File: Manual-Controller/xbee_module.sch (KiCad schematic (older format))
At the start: 7 parts, among them U7 TXB0104D, U8 XBee_SMT

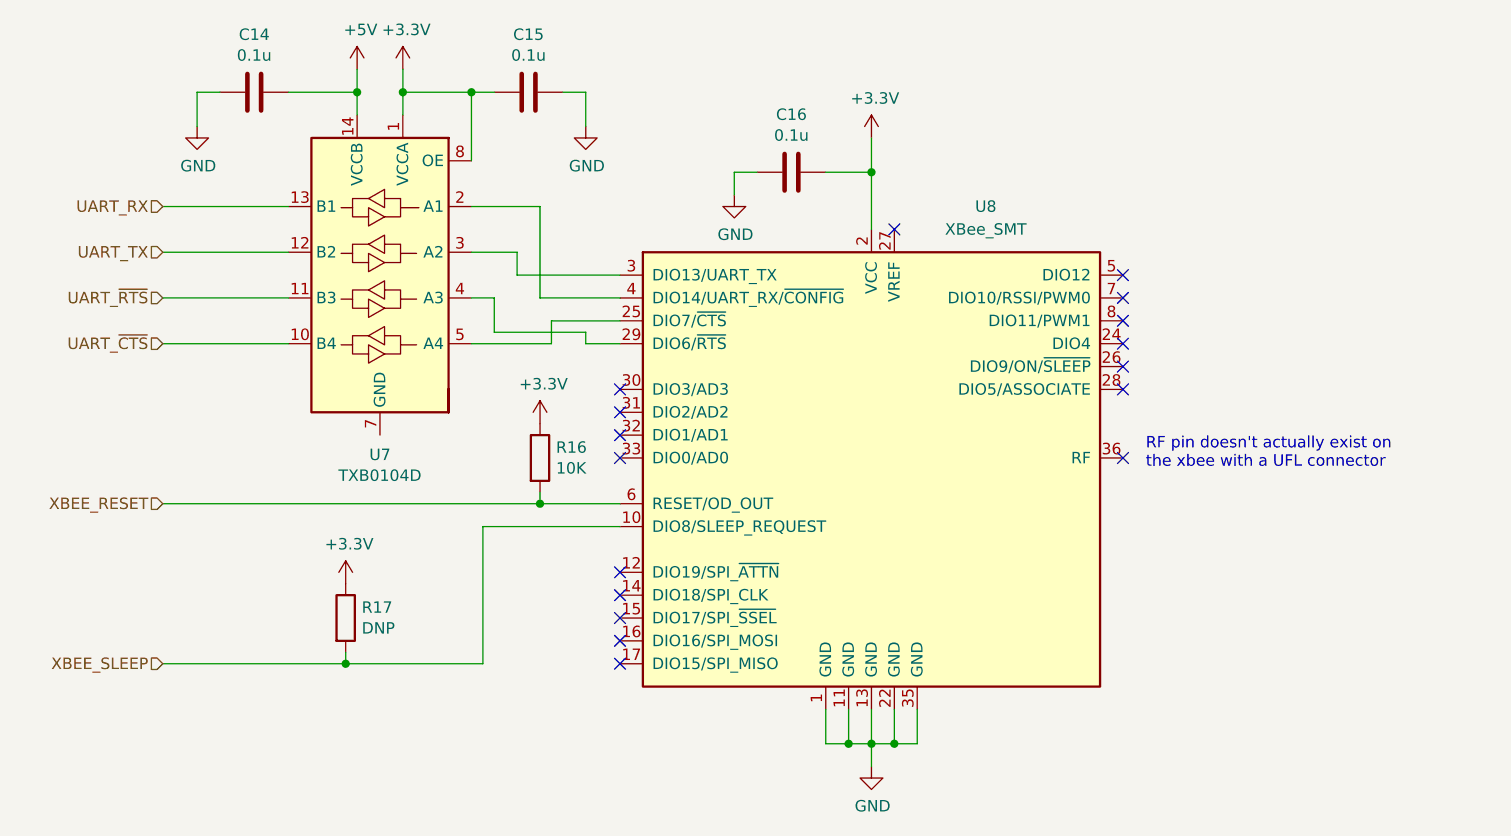
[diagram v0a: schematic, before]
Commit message: assined footprints and fixed pins
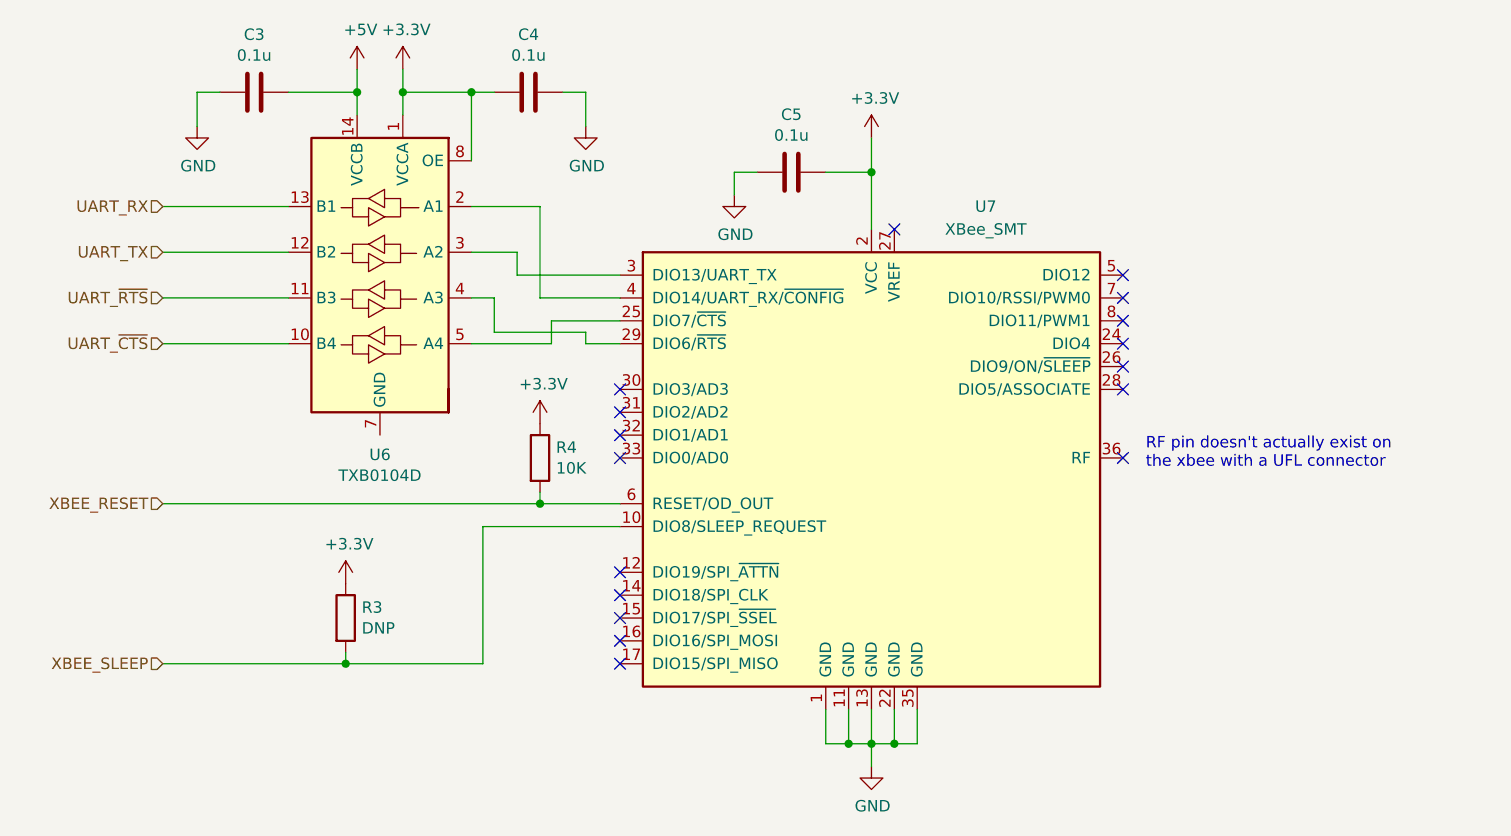
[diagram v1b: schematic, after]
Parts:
- C3: renamed from C14; footprint Capacitor_SMD:C_0805_2012Metric_Pad1.15x1.40mm_HandSolder -> Capacitor_SMD:C_0805_2012Metric_Pad1.18x1.45mm_HandSolder
- C4: renamed from C15; footprint Capacitor_SMD:C_0805_2012Metric_Pad1.15x1.40mm_HandSolder -> Capacitor_SMD:C_0805_2012Metric_Pad1.18x1.45mm_HandSolder
- C5: renamed from C16; footprint Capacitor_SMD:C_0805_2012Metric_Pad1.15x1.40mm_HandSolder -> Capacitor_SMD:C_0805_2012Metric_Pad1.18x1.45mm_HandSolder
- R3: renamed from R17; footprint Resistor_SMD:R_0805_2012Metric_Pad1.15x1.40mm_HandSolder -> Resistor_SMD:R_0805_2012Metric_Pad1.20x1.40mm_HandSolder
- R4: renamed from R16; footprint Resistor_SMD:R_0805_2012Metric_Pad1.15x1.40mm_HandSolder -> Resistor_SMD:R_0805_2012Metric_Pad1.20x1.40mm_HandSolder
- renumbered U7 to U6, U8 to U7
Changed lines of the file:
@@
 $Descr A4 11693 8268
 encoding utf-8
-Sheet 1 2
+Sheet 2 2
 Title ""
 Date ""
@@
 $EndDescr
 $Comp
-L RF_ZigBee:XBee_SMT U8
+L RF_ZigBee:XBee_SMT U7
 U 1 1 5BA27C8A
 P 6150 4250
-F 0 "U8" H 6650 5350 50  0000 C CNN
+F 0 "U7" H 6650 5350 50  0000 C CNN
 F 1 "XBee_SMT" H 6650 5250 50  0000 C CNN
 F 2 "RF_Module:Digi_XBee_SMT" H 6990 3190 50  0001 C CNN
@@
 $EndComp
 $Comp
-L Logic_LevelTranslator:TXB0104D U7
+L Logic_LevelTranslator:TXB0104D U6
 U 1 1 5BA28032
 P 4000 3450
-F 0 "U7" H 4000 2664 50  0000 C CNN
+F 0 "U6" H 4000 2664 50  0000 C CNN
 F 1 "TXB0104D" H 4000 2573 50  0000 C CNN
 F 2 "Package_SO:SOIC-14_3.9x8.7mm_P1.27mm" H 4000 2700 50  0001 C CNN
@@
 $EndComp
 $Comp
-L power:+3.3V #PWR048
+L power:+3.3V #PWR027
 U 1 1 5BA280E0
 P 4100 2550
-F 0 "#PWR048" H 4100 2400 50  0001 C CNN
+F 0 "#PWR027" H 4100 2400 50  0001 C CNN
 F 1 "+3.3V" H 4115 2723 50  0000 C CNN
 F 2 "" H 4100 2550 50  0001 C CNN
@@
 Connection ~ 4100 2650
 $Comp
-L power:+5V #PWR047
+L power:+5V #PWR026
 U 1 1 5BA28183
 P 3900 2550
-F 0 "#PWR047" H 3900 2400 50  0001 C CNN
+F 0 "#PWR026" H 3900 2400 50  0001 C CNN
 F 1 "+5V" H 3915 2723 50  0000 C CNN
 F 2 "" H 3900 2550 50  0001 C CNN
@@
 $EndComp
 $Comp
-L Device:C C15
+L Device:C C4
 U 1 1 5BA281C0
 P 4650 2650
-F 0 "C15" V 4398 2650 50  0000 C CNN
+F 0 "C4" V 4398 2650 50  0000 C CNN
 F 1 "0.1u" V 4489 2650 50  0000 C CNN
-F 2 "Capacitor_SMD:C_0805_2012Metric_Pad1.15x1.40mm_HandSolder" H 4688 2500 50  0001 C CNN
+F 2 "Capacitor_SMD:C_0805_2012Metric_Pad1.18x1.45mm_HandSolder" H 4688 2500 50  0001 C CNN
 F 3 "~" H 4650 2650 50  0001 C CNN
 	1    4650 2650
@@
 $EndComp
 $Comp
-L power:GND #PWR050
+L power:GND #PWR029
 U 1 1 5BA2824E
 P 4900 2800
-F 0 "#PWR050" H 4900 2550 50  0001 C CNN
+F 0 "#PWR029" H 4900 2550 50  0001 C CNN
 F 1 "GND" H 4905 2627 50  0000 C CNN
 F 2 "" H 4900 2800 50  0001 C CNN
@@
 Connection ~ 4400 2650
 $Comp
-L Device:C C14
+L Device:C C3
 U 1 1 5BA282BA
 P 3450 2650
-F 0 "C14" V 3198 2650 50  0000 C CNN
+F 0 "C3" V 3198 2650 50  0000 C CNN
 F 1 "0.1u" V 3289 2650 50  0000 C CNN
-F 2 "Capacitor_SMD:C_0805_2012Metric_Pad1.15x1.40mm_HandSolder" H 3488 2500 50  0001 C CNN
+F 2 "Capacitor_SMD:C_0805_2012Metric_Pad1.18x1.45mm_HandSolder" H 3488 2500 50  0001 C CNN
 F 3 "~" H 3450 2650 50  0001 C CNN
 	1    3450 2650
@@
 $EndComp
 $Comp
-L power:GND #PWR049
+L power:GND #PWR024
 U 1 1 5BA282FE
 P 3200 2800
-F 0 "#PWR049" H 3200 2550 50  0001 C CNN
+F 0 "#PWR024" H 3200 2550 50  0001 C CNN
 F 1 "GND" H 3205 2627 50  0000 C CNN
 F 2 "" H 3200 2800 50  0001 C CNN
@@
 NoConn ~ 6250 3250
 $Comp
-L power:+3.3V #PWR051
+L power:+3.3V #PWR031
 U 1 1 5BA28D48
 P 6150 2850
-F 0 "#PWR051" H 6150 2700 50  0001 C CNN
+F 0 "#PWR031" H 6150 2700 50  0001 C CNN
 F 1 "+3.3V" H 6165 3023 50  0000 C CNN
 F 2 "" H 6150 2850 50  0001 C CNN
@@
 NoConn ~ 7250 3450
 $Comp
-L power:GND #PWR055
+L power:GND #PWR032
 U 1 1 5BA2AF15
 P 6150 5600
-F 0 "#PWR055" H 6150 5350 50  0001 C CNN
+F 0 "#PWR032" H 6150 5350 50  0001 C CNN
 F 1 "GND" H 6155 5427 50  0000 C CNN
 F 2 "" H 6150 5600 50  0001 C CNN
@@
 	3050 3150 3600 3150
 $Comp
-L Device:R R16
+L Device:R R4
 U 1 1 5BA2D660
 P 4700 4250
-F 0 "R16" H 4770 4296 50  0000 L CNN
+F 0 "R4" H 4770 4296 50  0000 L CNN
 F 1 "10K" H 4770 4205 50  0000 L CNN
-F 2 "Resistor_SMD:R_0805_2012Metric_Pad1.15x1.40mm_HandSolder" V 4630 4250 50  0001 C CNN
+F 2 "Resistor_SMD:R_0805_2012Metric_Pad1.20x1.40mm_HandSolder" V 4630 4250 50  0001 C CNN
 F 3 "~" H 4700 4250 50  0001 C CNN
 	1    4700 4250
@@
 $EndComp
 $Comp
-L power:+3.3V #PWR053
+L power:+3.3V #PWR028
 U 1 1 5BA2D6C9
 P 4700 4100
-F 0 "#PWR053" H 4700 3950 50  0001 C CNN
+F 0 "#PWR028" H 4700 3950 50  0001 C CNN
 F 1 "+3.3V" H 4715 4273 50  0000 C CNN
 F 2 "" H 4700 4100 50  0001 C CNN
@@
 NoConn ~ 7250 3850
 $Comp
-L Device:R R17
+L Device:R R3
 U 1 1 5BA2F17A
 P 3850 4950
-F 0 "R17" H 3920 4996 50  0000 L CNN
+F 0 "R3" H 3920 4996 50  0000 L CNN
 F 1 "DNP" H 3920 4905 50  0000 L CNN
-F 2 "Resistor_SMD:R_0805_2012Metric_Pad1.15x1.40mm_HandSolder" V 3780 4950 50  0001 C CNN
+F 2 "Resistor_SMD:R_0805_2012Metric_Pad1.20x1.40mm_HandSolder" V 3780 4950 50  0001 C CNN
 F 3 "~" H 3850 4950 50  0001 C CNN
 	1    3850 4950
@@
 $EndComp
 $Comp
-L power:+3.3V #PWR054
+L power:+3.3V #PWR025
 U 1 1 5BA2F202
 P 3850 4800
-F 0 "#PWR054" H 3850 4650 50  0001 C CNN
+F 0 "#PWR025" H 3850 4650 50  0001 C CNN
 F 1 "+3.3V" H 3865 4973 50  0000 C CNN
 F 2 "" H 3850 4800 50  0001 C CNN
@@
 Connection ~ 3850 5150
 $Comp
-L Device:C C16
+L Device:C C5
 U 1 1 5B9F00A1
 P 5800 3000
-F 0 "C16" V 5548 3000 50  0000 C CNN
+F 0 "C5" V 5548 3000 50  0000 C CNN
 F 1 "0.1u" V 5639 3000 50  0000 C CNN
-F 2 "Capacitor_SMD:C_0805_2012Metric_Pad1.15x1.40mm_HandSolder" H 5838 2850 50  0001 C CNN
+F 2 "Capacitor_SMD:C_0805_2012Metric_Pad1.18x1.45mm_HandSolder" H 5838 2850 50  0001 C CNN
 F 3 "~" H 5800 3000 50  0001 C CNN
 	1    5800 3000
@@
 	6150 3000 6150 3250
 $Comp
-L power:GND #PWR052
+L power:GND #PWR030
 U 1 1 5B9F12A1
 P 5550 3100
-F 0 "#PWR052" H 5550 2850 50  0001 C CNN
+F 0 "#PWR030" H 5550 2850 50  0001 C CNN
 F 1 "GND" H 5555 2927 50  0000 C CNN
 F 2 "" H 5550 3100 50  0001 C CNN

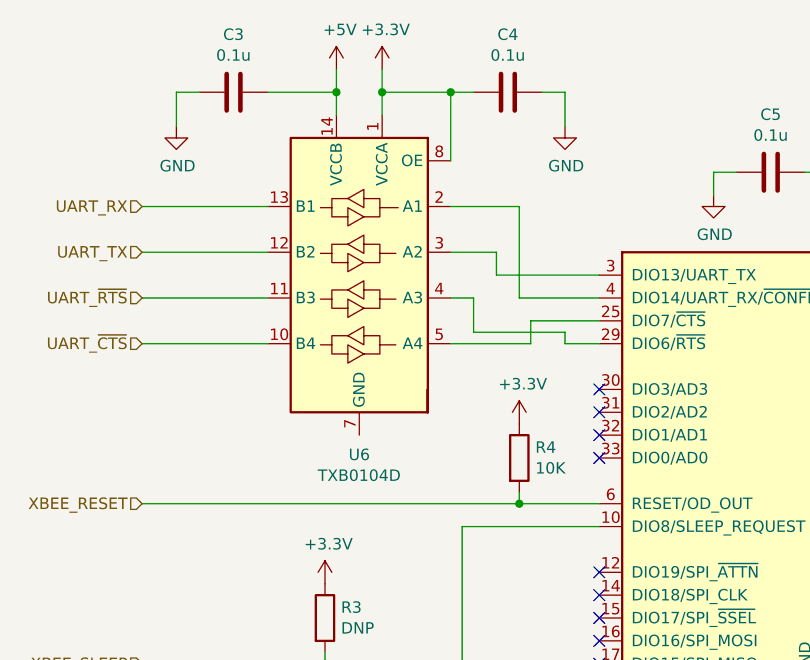
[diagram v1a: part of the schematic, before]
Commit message: finish schematic v1
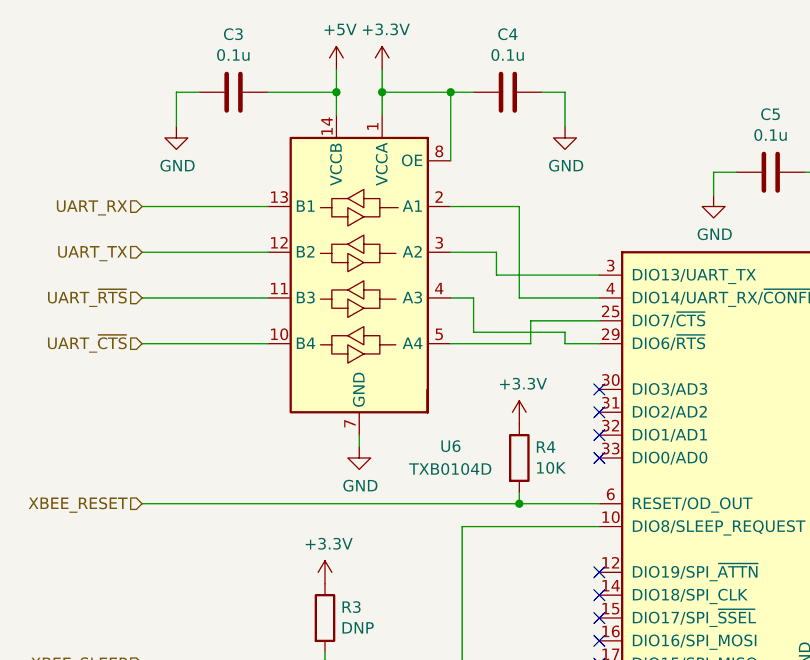
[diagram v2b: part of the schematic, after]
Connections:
- net GND: now also U6.7 (GND)
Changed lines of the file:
@@
 U 1 1 5BA28032
 P 4000 3450
-F 0 "U6" H 4000 2664 50  0000 C CNN
-F 1 "TXB0104D" H 4000 2573 50  0000 C CNN
+F 0 "U6" H 3600 2700 50  0000 C CNN
+F 1 "TXB0104D" H 3600 2600 50  0000 C CNN
 F 2 "Package_SO:SOIC-14_3.9x8.7mm_P1.27mm" H 4000 2700 50  0001 C CNN
 F 3 "http://www.ti.com/lit/ds/symlink/txb0104.pdf" H 4110 3545 50  0001 C CNN
@@
 Wire Wire Line
 	3200 2650 3300 2650
-Wire Wire Line
-	3600 2650 3900 2650
-Wire Wire Line
-	3900 2650 3900 2550
-Wire Wire Line
-	3900 2650 3900 2750
-Connection ~ 3900 2650
 Wire Wire Line
 	4400 3550 4500 3550
@@
 Wire Wire Line
 	4600 3450 5050 3450
+$Comp
+L power:GND #PWR035
+U 1 1 61CC701E
+P 4000 4200
+F 0 "#PWR035" H 4000 3950 50  0001 C CNN
+F 1 "GND" H 4005 4027 50  0000 C CNN
+F 2 "" H 4000 4200 50  0001 C CNN
+F 3 "" H 4000 4200 50  0001 C CNN
+	1    4000 4200
+	1    0    0    -1
+$EndComp
+Wire Wire Line
+	4000 4150 4000 4200
+Wire Wire Line
+	3900 2550 3900 2650
+Wire Wire Line
+	3600 2650 3900 2650
+Wire Wire Line
+	3900 2650 3900 2750
+Connection ~ 3900 2650
 $EndSCHEMATC
